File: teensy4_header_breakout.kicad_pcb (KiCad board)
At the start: 2 copper layers, 22.9 x 35.6 mm, 3 parts, among them J1 Conn_01x14, J2 Conn_01x14, U1 GND-1

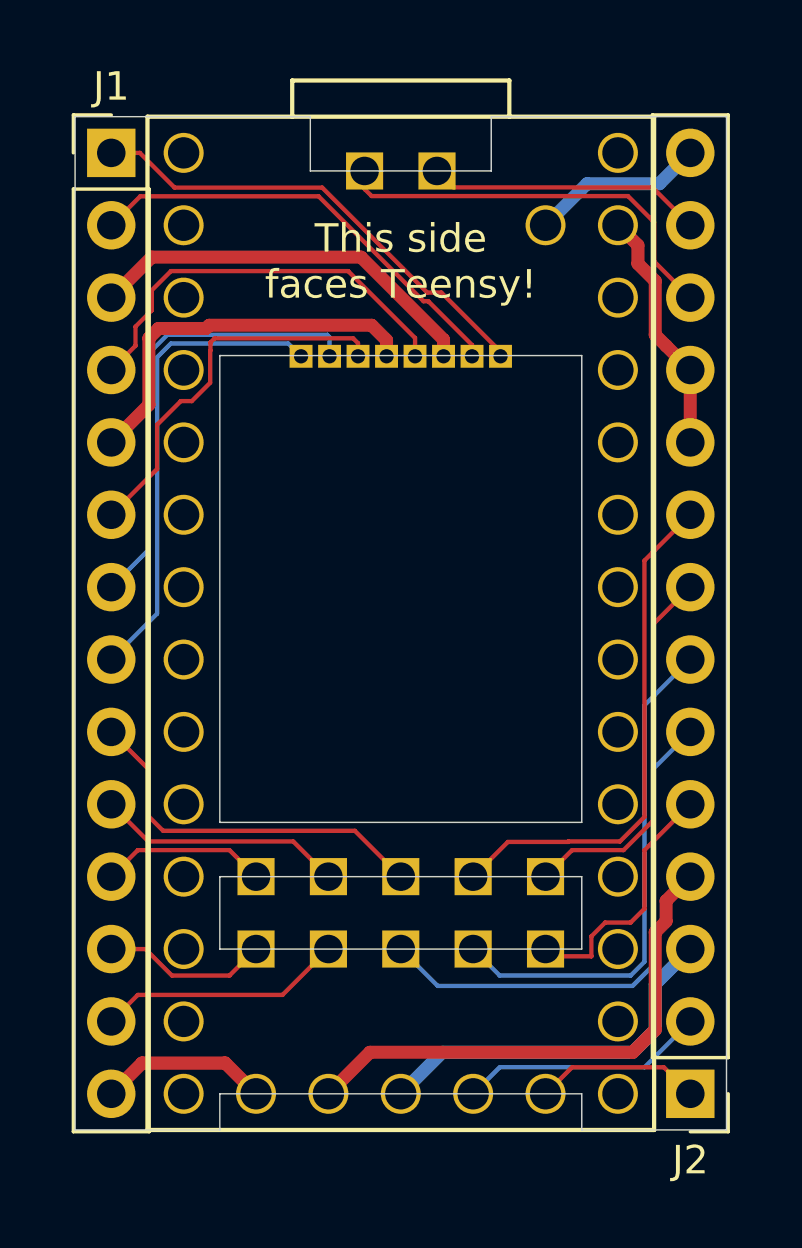
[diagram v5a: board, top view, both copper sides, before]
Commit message: Added ground plane and graphics for sidecars
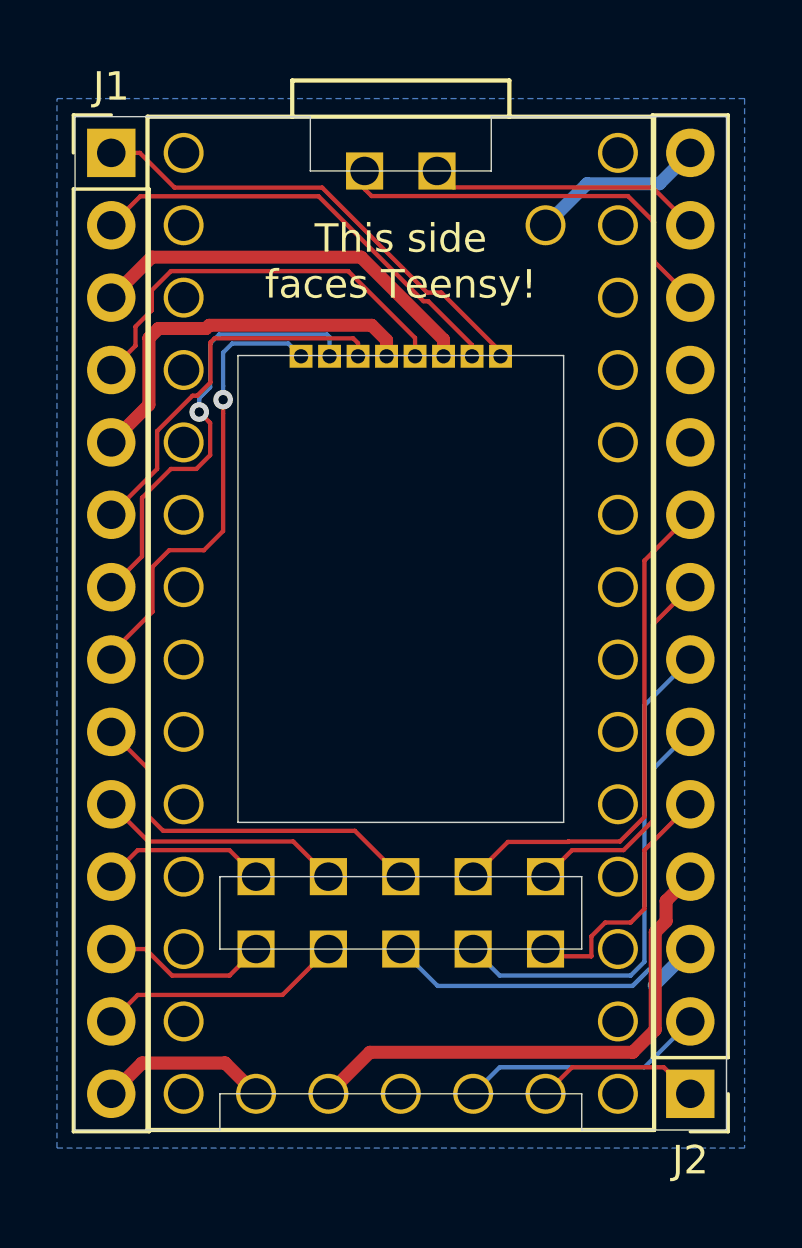
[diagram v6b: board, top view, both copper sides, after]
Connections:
- J1 pad 3: /GND-SD -> /GND
- J2 pad 3: /GND-1 -> /GND
- U1 pad 17: /GND-1 -> /GND
- U1 pad 47: /GND-SD -> /GND
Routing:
- net /GND-SD: track 14.1 -> 0.00 mm
- net /GND-1: track 12.6 -> 0.00 mm
- net /GND: track 8.67 -> 15.9 mm
- net /DAT2: track 16.3 -> 15.8 mm, vias 0 -> 1
- net /DAT3: track 15.8 -> 15.6 mm, vias 0 -> 1
- added copper zone on B.Cu, net /GND
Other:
- outline, holes or cut-outs redrawn
- net class Power: trace_width 0.3048 -> 0.4572
- board text added: "2019-10-22"
- board text added: "ESP"
- board text added: "SD"
- board text added: "USB"
- board text removed: "2019-10-20"

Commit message: Fix date
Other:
- board text added: "2019-10-21"
- board text removed: "2019-10-22"
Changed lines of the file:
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@@
     (add_net /VBAT)
     (add_net /VUSB)
-    (add_net "Net-(U1-Pad1)")
-    (add_net "Net-(U1-Pad10)")
-    (add_net "Net-(U1-Pad11)")
-    (add_net "Net-(U1-Pad12)")
-    (add_net "Net-(U1-Pad13)")
-    (add_net "Net-(U1-Pad14)")
-    (add_net "Net-(U1-Pad2)")
-    (add_net "Net-(U1-Pad20)")
-    (add_net "Net-(U1-Pad21)")
-    (add_net "Net-(U1-Pad22)")
-    (add_net "Net-(U1-Pad23)")
-    (add_net "Net-(U1-Pad24)")
-    (add_net "Net-(U1-Pad25)")
-    (add_net "Net-(U1-Pad26)")
-    (add_net "Net-(U1-Pad27)")
-    (add_net "Net-(U1-Pad28)")
-    (add_net "Net-(U1-Pad29)")
-    (add_net "Net-(U1-Pad3)")
-    (add_net "Net-(U1-Pad30)")
-    (add_net "Net-(U1-Pad31)")
-    (add_net "Net-(U1-Pad33)")
-    (add_net "Net-(U1-Pad4)")
-    (add_net "Net-(U1-Pad5)")
-    (add_net "Net-(U1-Pad6)")
-    (add_net "Net-(U1-Pad7)")
-    (add_net "Net-(U1-Pad8)")
-    (add_net "Net-(U1-Pad9)")
   )
   (net_class Power ""
@@
     (descr "Through hole straight pin header, 1x14, 2.54mm pitch, single row")
     (tags "Through hole pin header THT 1x14 2.54mm single row")
-    (fp_text reference J2 (at 0 -2.33) (layer F.SilkS)
+    (fp_text reference J2 (at 0 -2.33) (layer F.SilkS) hide
       (effects (font (size 1 1) (thickness 0.15)))
     )
@@
     (descr "Through hole straight pin header, 1x14, 2.54mm pitch, single row")
     (tags "Through hole pin header THT 1x14 2.54mm single row")
-    (fp_text reference J1 (at 0 -2.33) (layer F.SilkS)
+    (fp_text reference J1 (at 0 -2.33) (layer F.SilkS) hide
       (effects (font (size 1 1) (thickness 0.15)))
     )
@@
   (gr_circle (center 161.29 81.915) (end 161.671 82.931) (layer B.SilkS) (width 0.12))
   (gr_circle (center 165.1 83.82) (end 165.354 85.09) (layer B.SilkS) (width 0.12))
-  (gr_text 2019-10-22 (at 159.9438 111.6584) (layer B.SilkS)
+  (gr_text 2019-10-21 (at 159.9438 111.6584) (layer B.SilkS)
     (effects (font (size 1.27 1.27) (thickness 0.2032)) (justify mirror))
   )

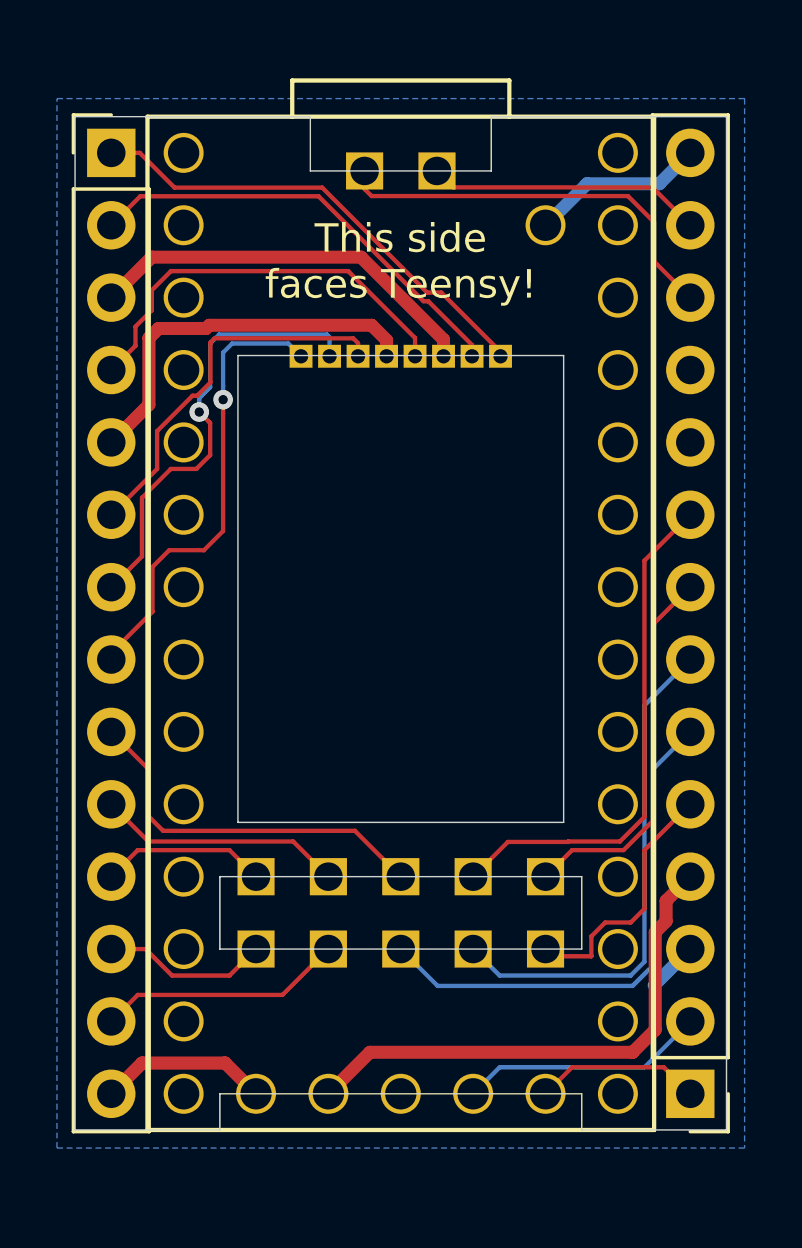
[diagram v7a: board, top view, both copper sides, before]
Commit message: Add gnd pin to plane
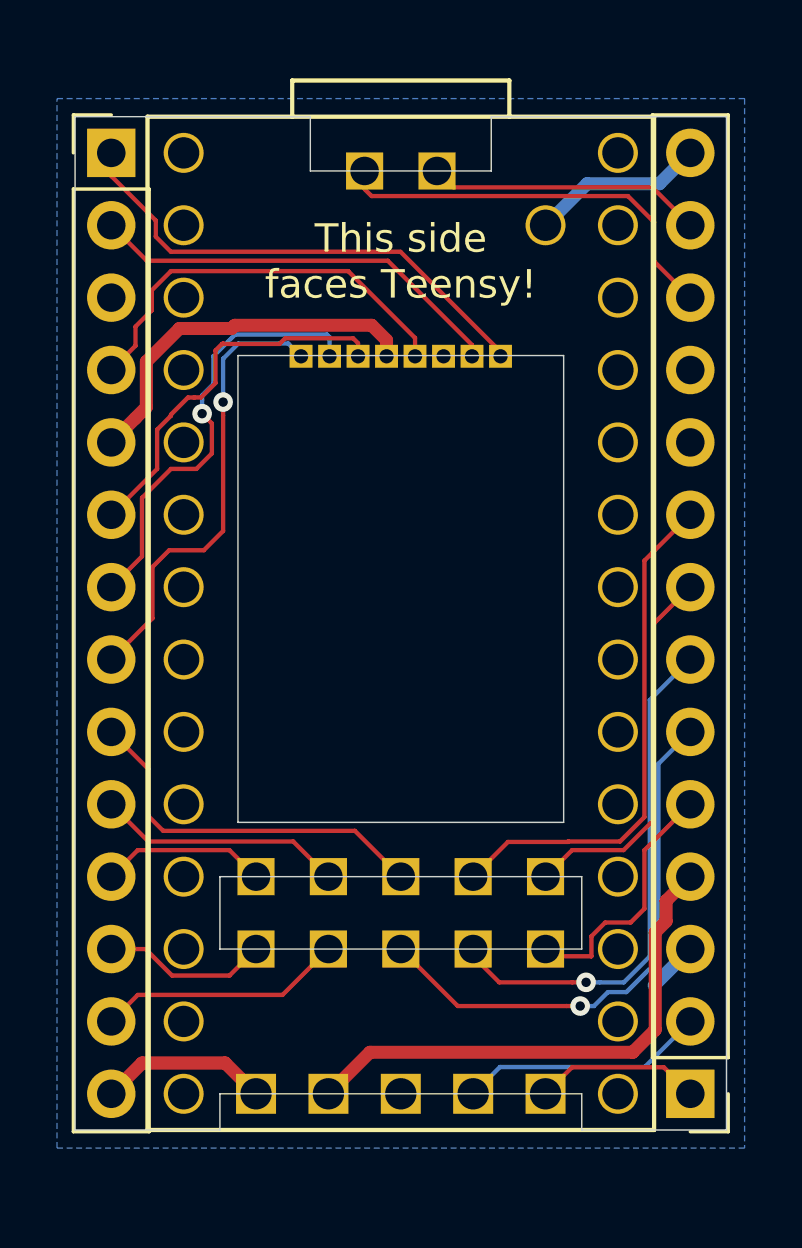
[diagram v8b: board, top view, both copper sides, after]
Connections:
- U1 pad 1: (no net) -> /GND
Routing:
- net /GND: track 15.9 -> 1.85 mm
- net /DAT0: track 15.4 -> 14.5 mm
- net /DAT1: track 16.5 -> 17.3 mm
- net /28: track 18.1 -> 18.6 mm, vias 0 -> 1
- net /26: track 17.5 -> 18.0 mm, vias 0 -> 1
